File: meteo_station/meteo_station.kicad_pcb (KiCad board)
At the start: 2 copper layers, 110 x 90 mm, 26 parts, among them SW1 SW_SPDT, U1 TP4056, U2 LF33_TO220, U3 ESP32-WROOM, U4 DS18B20, U5 BH1750, U6 BME280

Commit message: Add jumper & version
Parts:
- removed the G*** at (148.6, 99.7)
- removed R6: 0R, Resistor_SMD:R_0603_1608Metric
- added G***: LOGO, meteo_station_footprints:version, F.Cu at (189.2, 83.8)
- added JP1: SolderJumper, Jumper:SolderJumper-2_P1.3mm_Bridged_Pad1.0x1.5mm, F.Cu at (127.0, 99.1)
- moved C2 3.17 mm to (126.4, 120.7)
- moved C3 3.17 mm to (126.4, 115.6)
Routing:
- net GND: track 57.0 -> 63.7 mm
- net OUT+: track 86.8 -> 83.7 mm
- net 3V3: track 175.3 -> 172.1 mm
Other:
- board text removed: "lorem ipsum"

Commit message: Add images
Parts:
- added G***: LOGO, meteo_station_footprints:meteo_station_small, F.Cu at (186.9, 75.9)
- added G***: LOGO, meteo_station_footprints:chmurka2_small, F.Cu at (96.5, 130.0)
- added G***: LOGO, meteo_station_footprints:chmurka, F.Cu at (173.0, 59.7)
- added G***: LOGO, meteo_station_footprints:chmurka, B.Cu at (167.1, 76.2)
- added G***: LOGO, meteo_station_footprints:chmurka, B.Cu at (197.5, 151.6)
- added G***: LOGO, meteo_station_footprints:meteo_station, B.Cu at (149.9, 144.8)
- added G***: LOGO, meteo_station_footprints:chmurka2, B.Cu at (200.7, 100.3)
- added G***: LOGO, meteo_station_footprints:chmurka2, B.Cu at (101.2, 118.7)
- G***: moved to B.Cu
- moved G*** 78.8 mm to (133.3, 139.4), turned to 180 degrees

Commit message: Delete ALL tracks
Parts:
- added C4: 2.2uF, Capacitor_Tantalum_SMD:CP_EIA-3216-18_Kemet-A, F.Cu at (126.4, 80.0)
- added C5: 100nF, Capacitor_SMD:C_0603_1608Metric, F.Cu at (198.8, 108.6)
- C1: value 100nF -> 2200uF; footprint Capacitor_SMD:C_0603_1608Metric -> Capacitor_THT:CP_Radial_D10.0mm_P5.00mm
- C3: value 2.2uF -> 100nF; footprint Capacitor_Tantalum_SMD:CP_EIA-3216-18_Kemet-A -> Capacitor_SMD:C_0603_1608Metric
- moved SC2 69.8 mm to (58.8, 64.8)
- moved D2 57.7 mm to (70.6, 81.9)
- moved SW1 57.5 mm to (47.0, 81.3)
- moved SC1 57.1 mm to (58.8, 73.7)
- moved D1 57.0 mm to (58.8, 81.9)
- moved C2 41.5 mm to (144.1, 83.2)
- moved U2 35.6 mm to (120.1, 85.1)
- moved C1 32.8 mm to (127.6, 72.1)
- moved C3 30.5 mm to (126.4, 85.1)
- moved JP1 1.27 mm to (127.0, 100.3)
- moved U1 1.27 mm to (113.0, 100.3)
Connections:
- C1 pad 1: BAT_V -> 3V3
- C2 pad 1: OUT+ -> BAT_V
- C3 pad 1: 3V3 -> OUT+
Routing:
- net 3V3: track 172.1 -> 0.00 mm
- net Net-(R5-Pad2): track 126.4 -> 0.00 mm, vias 1 -> 0
- net SDA: track 95.4 -> 0.00 mm, vias 1 -> 0
- net Net-(BT1-Pad1): track 94.4 -> 0.00 mm
- net OUT+: track 83.7 -> 0.00 mm, vias 1 -> 0
- net SCL: track 74.2 -> 0.00 mm, vias 1 -> 0
- net Net-(SC1-Pad2): track 74.0 -> 0.00 mm
- net GND: track 63.7 -> 0.00 mm, vias 2 -> 0
- net Net-(D1-Pad1): track 59.7 -> 0.00 mm, vias 2 -> 0
- net BAT_V: track 59.6 -> 0.00 mm
- net Net-(BT1-Pad2): track 45.3 -> 0.00 mm
- net Net-(SW1-Pad2): track 25.7 -> 0.00 mm
- net OUT-: track 13.6 -> 0.00 mm
- net Net-(D2-Pad2): track 11.3 -> 0.00 mm
- net Net-(D1-Pad2): track 11.3 -> 0.00 mm

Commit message: Finished moving
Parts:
- moved SC2 83.5 mm to (120.7, 120.9)
- moved SC1 71.0 mm to (111.8, 120.9)
- moved D2 69.8 mm to (128.9, 120.4)
- moved SW1 66.7 mm to (112.8, 92.1), turned to 180 degrees
- moved D1 58.7 mm to (103.1, 120.4)
- moved C3 23.3 mm to (103.1, 83.8), turned to 180 degrees
- moved U2 9.90 mm to (110.2, 83.8), turned to 0 degrees
- moved JP1 6.38 mm to (127.6, 106.7)
- moved U1 6.35 mm to (113.0, 106.7)
- moved C4 4.96 mm to (123.2, 83.8)
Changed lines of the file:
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@@
   )
   (footprint "meteo_station_footprints:SolarPanel_JST" (layer "F.Cu")
-    (at 58.801 73.66)
+    (at 111.76 120.904)
     (property "Sheetfile" "meteo_station.kicad_sch")
     (property "Sheetname" "")
     (attr through_hole)
-    (fp_text reference "SC1" (at -5.715 0 unlocked) (layer "F.SilkS")
+    (fp_text reference "SC1" (at -0.016 -3.556 unlocked) (layer "F.SilkS")
       (effects (font (size 0.8 0.8) (thickness 0.15)))
     )
-    (fp_text value "Solar_Cell" (at -8.255 -1.905 unlocked) (layer "F.SilkS")
+    (fp_text value "Solar_Cell" (at 0 -3.556 unlocked) (layer "F.SilkS") hide
       (effects (font (size 1 1) (thickness 0.15)))
     )
@@
   )
   (footprint "Package_TO_SOT_THT:TO-220-3_Horizontal_TabDown" (layer "F.Cu")
-    (at 120.055 85.09 90)
+    (at 110.236 83.82)
     (descr "TO-220-3, Horizontal, RM 2.54mm, see https://www.vishay.com/docs/66542/to-220-1.pdf")
     (tags "TO-220-3 Horizontal RM 2.54mm")
@@
     (property "Sheetname" "")
     (attr through_hole)
-    (fp_text reference "U2" (at 8.89 -18.755) (layer "F.SilkS")
+    (fp_text reference "U2" (at -2.032 -20.32 180) (layer "F.SilkS")
       (effects (font (size 0.8 0.8) (thickness 0.15)))
     )
-    (fp_text value "LF33_TO220" (at 2.54 2 90) (layer "F.Fab")
+    (fp_text value "LF33_TO220" (at 2.54 2) (layer "F.Fab")
       (effects (font (size 1 1) (thickness 0.15)))
     )
-    (fp_text user "${REFERENCE}" (at 2.54 -20.58 90) (layer "F.Fab")
+    (fp_text user "${REFERENCE}" (at 2.54 -20.58) (layer "F.Fab")
       (effects (font (size 1 1) (thickness 0.15)))
     )
@@
     (fp_line (start -2.46 -3.81) (end -2.46 -13.06) (layer "F.Fab") (width 0.1))
     (fp_circle (center 2.54 -16.66) (end 4.39 -16.66) (layer "F.Fab") (width 0.1) (fill none))
-    (pad "" np_thru_hole oval locked (at 2.54 -16.66 90) (size 3.5 3.5) (drill 3.5) (layers *.Cu *.Mask))
-    (pad "1" thru_hole rect locked (at 0 0 90) (size 1.905 2) (drill 1.1) (layers *.Cu *.Mask)
+    (pad "" np_thru_hole oval locked (at 2.54 -16.66) (size 3.5 3.5) (drill 3.5) (layers *.Cu *.Mask))
+    (pad "1" thru_hole rect locked (at 0 0) (size 1.905 2) (drill 1.1) (layers *.Cu *.Mask)
       (net 11 "OUT+") (pinfunction "VI") (pintype "passive"))
-    (pad "2" thru_hole oval locked (at 2.54 0 90) (size 1.905 2) (drill 1.1) (layers *.Cu *.Mask)
+    (pad "2" thru_hole oval locked (at 2.54 0) (size 1.905 2) (drill 1.1) (layers *.Cu *.Mask)
       (net 39 "GND") (pinfunction "GND") (pintype "power_in"))
-    (pad "3" thru_hole oval locked (at 5.08 0 90) (size 1.905 2) (drill 1.1) (layers *.Cu *.Mask)
+    (pad "3" thru_hole oval locked (at 5.08 0) (size 1.905 2) (drill 1.1) (layers *.Cu *.Mask)
       (net 3 "3V3") (pinfunction "VO") (pintype "passive"))
     (model "${KICAD6_3DMODEL_DIR}/Package_TO_SOT_THT.3dshapes/TO-220-3_Horizontal_TabDown.wrl"
@@
   )
   (footprint "Diode_SMD:D_SMB" (layer "F.Cu")
-    (at 70.621 81.915 180)
+    (at 128.905 120.396 180)
     (descr "Diode SMB (DO-214AA)")
     (tags "Diode SMB (DO-214AA)")
@@
   )
   (footprint "meteo_station_footprints:MTS102" (layer "F.Cu")
-    (at 46.99 81.28 90)
+    (at 112.776 92.075 180)
     (property "Sheetfile" "meteo_station.kicad_sch")
     (property "Sheetname" "")
     (attr through_hole)
-    (fp_text reference "SW1" (at -7.62 3.81 unlocked) (layer "F.SilkS")
+    (fp_text reference "SW1" (at 4.191 5.08 unlocked) (layer "F.SilkS")
       (effects (font (size 0.8 0.8) (thickness 0.15)) (justify right))
     )
-    (fp_text value "SW_SPDT" (at 0 -5.715 90 unlocked) (layer "F.Fab")
+    (fp_text value "SW_SPDT" (at -0.635 -5.715 180 unlocked) (layer "F.Fab")
       (effects (font (size 1 1) (thickness 0.15)))
     )
-    (fp_text user "${REFERENCE}" (at 0 -6.985 90 unlocked) (layer "F.Fab")
+    (fp_text user "${REFERENCE}" (at -0.635 -6.985 180 unlocked) (layer "F.Fab")
       (effects (font (size 1 1) (thickness 0.15)))
     )
     (fp_rect (start -6.6 -4) (end 6.6 4) (layer "F.SilkS") (width 0.2) (fill none))
-    (pad "1" thru_hole oval (at -4.7 0 90) (size 3.2 6.5) (drill oval 2 3) (layers *.Cu *.Mask)
+    (pad "1" thru_hole oval (at -4.7 0 180) (size 3.2 6.5) (drill oval 2 3) (layers *.Cu *.Mask)
       (net 11 "OUT+") (pinfunction "A") (pintype "passive"))
-    (pad "2" thru_hole oval (at 0 0 90) (size 3.2 6.5) (drill oval 2 3) (layers *.Cu *.Mask)
+    (pad "2" thru_hole oval (at 0 0 180) (size 3.2 6.5) (drill oval 2 3) (layers *.Cu *.Mask)
       (net 7 "Net-(SW1-Pad2)") (pinfunction "B") (pintype "passive"))
-    (pad "3" thru_hole oval (at 4.7 0 90) (size 3.2 6.5) (drill oval 2 3) (layers *.Cu *.Mask)
+    (pad "3" thru_hole oval (at 4.7 0 180) (size 3.2 6.5) (drill oval 2 3) (layers *.Cu *.Mask)
       (net 8 "unconnected-(SW1-Pad3)") (pinfunction "C") (pintype "passive+no_connect"))
   )
@@
   )
   (footprint "Jumper:SolderJumper-2_P1.3mm_Bridged_Pad1.0x1.5mm" (layer "F.Cu")
-    (at 127 100.33)
+    (at 127.635 106.68)
     (descr "SMD Solder Jumper, 1x1.5mm Pads, 0.3mm gap, bridged with 1 copper strip")
     (tags "net tie solder jumper bridged")
@@
   )
   (footprint "Capacitor_Tantalum_SMD:CP_EIA-3216-18_Kemet-A" (layer "F.Cu")
-    (at 126.365 80.01)
+    (at 123.19 83.82)
     (descr "Tantalum Capacitor SMD Kemet-A (3216-18 Metric), IPC_7351 nominal, (Body size from: http://www.kemet.com/Lists/ProductCatalog/Attachments/253/KEM_TC101_STD.pdf), generated with kicad-footprint-generator")
     (tags "capacitor tantalum")
@@
   )
   (footprint "Capacitor_SMD:C_0603_1608Metric" (layer "F.Cu")
-    (at 126.365 85.09)
+    (at 103.124 83.82 180)
     (descr "Capacitor SMD 0603 (1608 Metric), square (rectangular) end terminal, IPC_7351 nominal, (Body size source: IPC-SM-782 page 76, https://www.pcb-3d.com/wordpress/wp-content/uploads/ipc-sm-782a_amendment_1_and_2.pdf), generated with kicad-footprint-generator")
     (tags "capacitor")
@@
     (property "Sheetname" "")
     (attr smd)
-    (fp_text reference "C3" (at 0 -1.43) (layer "F.SilkS")
+    (fp_text reference "C3" (at 0 1.27) (layer "F.SilkS")
       (effects (font (size 0.8 0.8) (thickness 0.15)))
     )
@@
     (fp_line (start -0.8 -0.4) (end 0.8 -0.4) (layer "F.Fab") (width 0.1))
     (fp_line (start -0.8 0.4) (end -0.8 -0.4) (layer "F.Fab") (width 0.1))
-    (pad "1" smd roundrect locked (at -0.775 0) (size 0.9 0.95) (layers "F.Cu" "F.Paste" "F.Mask") (roundrect_rratio 0.25)
+    (pad "1" smd roundrect locked (at -0.775 0 180) (size 0.9 0.95) (layers "F.Cu" "F.Paste" "F.Mask") (roundrect_rratio 0.25)
       (net 11 "OUT+") (pintype "passive"))
-    (pad "2" smd roundrect locked (at 0.775 0) (size 0.9 0.95) (layers "F.Cu" "F.Paste" "F.Mask") (roundrect_rratio 0.25)
+    (pad "2" smd roundrect locked (at 0.775 0 180) (size 0.9 0.95) (layers "F.Cu" "F.Paste" "F.Mask") (roundrect_rratio 0.25)
       (net 39 "GND") (pintype "passive"))
     (model "${KICAD6_3DMODEL_DIR}/Capacitor_SMD.3dshapes/C_0603_1608Metric.wrl"
@@
   )
   (footprint "meteo_station_footprints:TP4056" (layer "F.Cu")
-    (at 113.03 100.33)
+    (at 113.03 106.68)
     (property "Sheetfile" "meteo_station.kicad_sch")
     (property "Sheetname" "")
     (attr through_hole)
-    (fp_text reference "U1" (at 12.5 9.525 unlocked) (layer "F.SilkS")
+    (fp_text reference "U1" (at -11.049 -9.398 unlocked) (layer "F.SilkS")
       (effects (font (size 0.8 0.8) (thickness 0.15)) (justify right))
     )
@@
   )
   (footprint "Diode_SMD:D_SMB" (layer "F.Cu")
-    (at 58.801 81.915 180)
+    (at 103.124 120.396 180)
     (descr "Diode SMB (DO-214AA)")
     (tags "Diode SMB (DO-214AA)")
@@
   )
   (footprint "meteo_station_footprints:SolarPanel_JST" (layer "F.Cu")
-    (at 58.801 64.77)
+    (at 120.65 120.904)
     (property "Sheetfile" "meteo_station.kicad_sch")
     (property "Sheetname" "")
     (attr through_hole)
-    (fp_text reference "SC2" (at -5.715 0 unlocked) (layer "F.SilkS")
+    (fp_text reference "SC2" (at -0.016 -3.556 unlocked) (layer "F.SilkS")
       (effects (font (size 0.8 0.8) (thickness 0.15)))
     )
-    (fp_text value "Solar_Cell" (at -8.255 -1.905 unlocked) (layer "F.SilkS")
+    (fp_text value "Solar_Cell" (at 0 -3.556 unlocked) (layer "F.SilkS") hide
       (effects (font (size 1 1) (thickness 0.15)))
     )

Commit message: new tracks
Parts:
- moved R5 38.3 mm to (132.7, 87.6)
- moved C2 27.6 mm to (167.0, 98.6), turned to -90 degrees
- moved R3 5.54 mm to (167.0, 87.6)
- moved R4 5.54 mm to (167.0, 93.2)
- turned R2 to -90 degrees
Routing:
- net 3V3: track 0.00 -> 166.9 mm
- net SDA: track 0.00 -> 106.3 mm, vias 0 -> 2
- net Net-(R5-Pad2): track 0.00 -> 100.3 mm
- net Net-(BT1-Pad1): track 0.00 -> 87.8 mm
- net SCL: track 0.00 -> 87.6 mm, vias 0 -> 1
- net BAT_V: track 0.00 -> 70.5 mm, vias 0 -> 1
- net Net-(D1-Pad1): track 0.00 -> 66.7 mm
- net Net-(BT1-Pad2): track 0.00 -> 45.5 mm
- net OUT+: track 0.00 -> 34.1 mm
- net Net-(SC1-Pad2): track 0.00 -> 27.8 mm
- net OUT-: track 0.00 -> 17.6 mm
- net Net-(SW1-Pad2): track 0.00 -> 15.7 mm
- net Net-(D1-Pad2): track 0.00 -> 13.1 mm
- net Net-(D2-Pad2): track 0.00 -> 10.5 mm

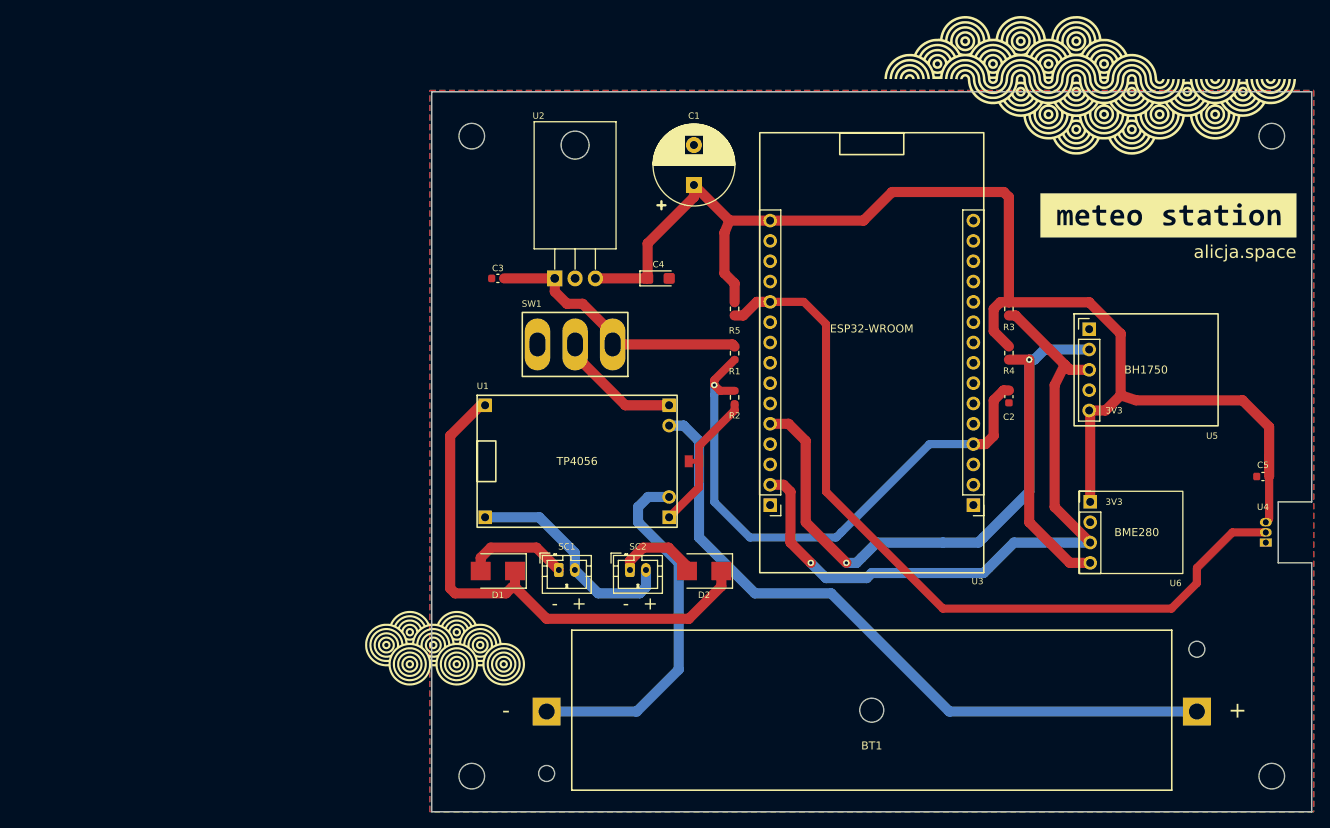
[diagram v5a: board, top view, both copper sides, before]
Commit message: Very thick routes
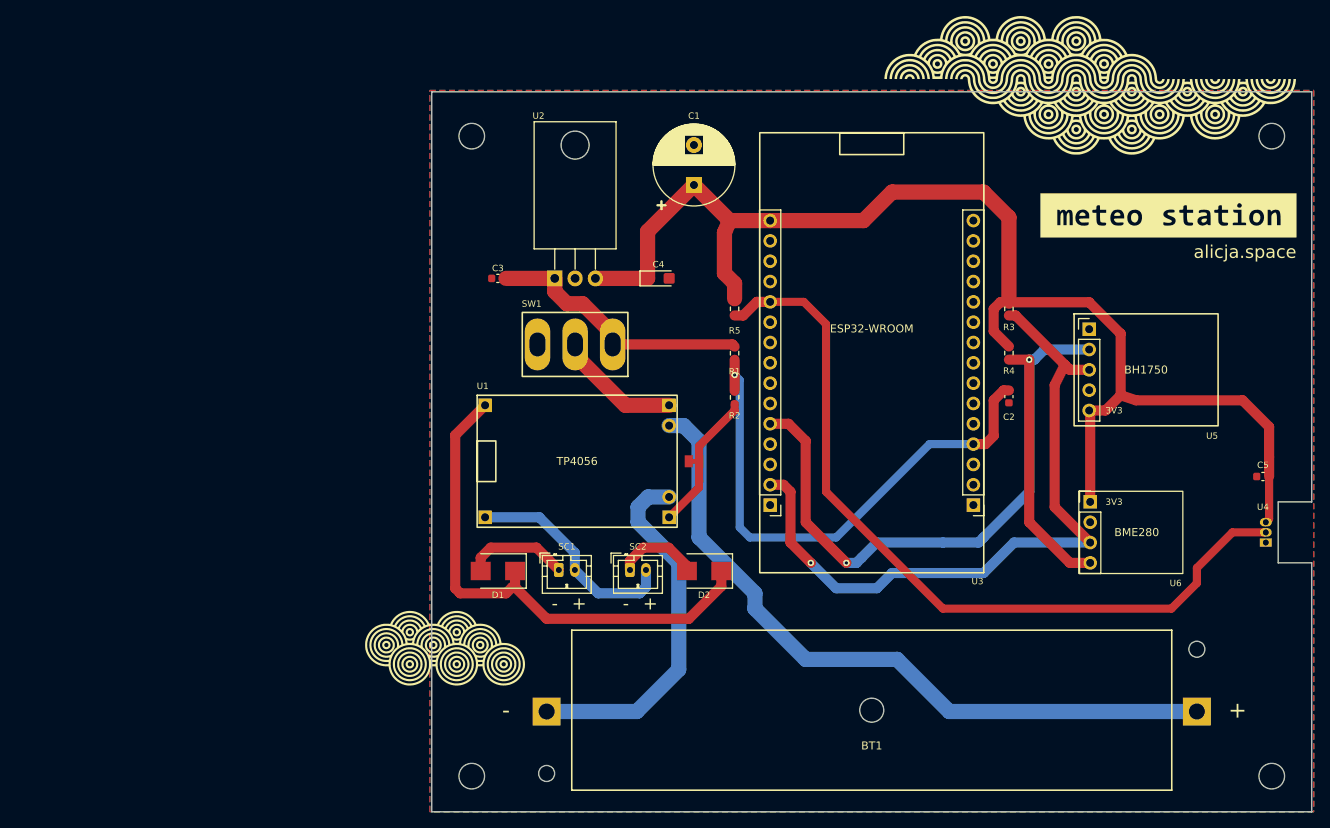
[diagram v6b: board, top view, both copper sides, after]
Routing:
- net BAT_V: track 70.5 -> 67.6 mm
- net 3V3: track 166.9 -> 164.9 mm
- net Net-(D1-Pad1): track 66.7 -> 65.5 mm
- net Net-(BT1-Pad1): track 87.8 -> 89.0 mm
- net SCL: track 87.6 -> 88.7 mm

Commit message: Typo & label
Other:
- board text added: "3V3"
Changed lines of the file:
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@@
       (outputformat 1)
       (mirror false)
-      (drillshape 1)
+      (drillshape 0)
       (scaleselection 1)
-      (outputdirectory "")
+      (outputdirectory "../gerbers/")
     )
   )
@@
     (fp_line (start -2.966 2.165) (end 2.934 2.165) (layer "F.Fab") (width 0.1))
     (fp_line (start -2.966 -2.335) (end -2.966 2.165) (layer "F.Fab") (width 0.1))
-    (pad "1" thru_hole roundrect (at -1.016 -0.635) (size 1.2 1.75) (drill 0.75) (layers *.Cu *.Mask) (roundrect_rratio 0.208333)
+    (pad "1" thru_hole roundrect (at -1.016 -0.635) (size 1.2 1.75) (drill 0.75) (layers *.Cu *.Mask) (roundrect_rratio 0.2083333333)
       (net 13 "Net-(D1-Pad2)") (pinfunction "+") (pintype "passive"))
     (pad "2" thru_hole oval (at 0.984 -0.635) (size 1.2 1.75) (drill 0.75) (layers *.Cu *.Mask)
@@
     (fp_line (start -1.6 0.8) (end 1.6 0.8) (layer "F.Fab") (width 0.1))
     (fp_line (start 1.6 -0.8) (end -1.2 -0.8) (layer "F.Fab") (width 0.1))
-    (pad "1" smd roundrect locked (at -1.35 0) (size 1.4 1.35) (layers "F.Cu" "F.Paste" "F.Mask") (roundrect_rratio 0.185185)
+    (pad "1" smd roundrect locked (at -1.35 0) (size 1.4 1.35) (layers "F.Cu" "F.Paste" "F.Mask") (roundrect_rratio 0.1851851852)
       (net 3 "3V3") (pintype "passive"))
-    (pad "2" smd roundrect locked (at 1.35 0) (size 1.4 1.35) (layers "F.Cu" "F.Paste" "F.Mask") (roundrect_rratio 0.185185)
+    (pad "2" smd roundrect locked (at 1.35 0) (size 1.4 1.35) (layers "F.Cu" "F.Paste" "F.Mask") (roundrect_rratio 0.1851851852)
       (net 39 "GND") (pintype "passive"))
     (model "${KICAD6_3DMODEL_DIR}/Capacitor_Tantalum_SMD.3dshapes/CP_EIA-3216-18_Kemet-A.wrl"
@@
     (fp_line (start -3.376 -2.745) (end -3.376 -1.495) (layer "F.Fab") (width 0.1))
     (fp_line (start -2.126 -2.745) (end -3.376 -2.745) (layer "F.Fab") (width 0.1))
-    (pad "1" thru_hole roundrect (at -1.016 -0.635) (size 1.2 1.75) (drill 0.75) (layers *.Cu *.Mask) (roundrect_rratio 0.208333)
+    (pad "1" thru_hole roundrect (at -1.016 -0.635) (size 1.2 1.75) (drill 0.75) (layers *.Cu *.Mask) (roundrect_rratio 0.2083333333)
       (net 14 "Net-(D2-Pad2)") (pinfunction "+") (pintype "passive"))
     (pad "2" thru_hole oval (at 0.984 -0.635) (size 1.2 1.75) (drill 0.75) (layers *.Cu *.Mask)
@@
   (gr_line (start 204.86 150.5) (end 204.86 119.38) (layer "Edge.Cuts") (width 0.1))
   (gr_line (start 204.86 60.5) (end 204.86 111.76) (layer "Edge.Cuts") (width 0.1))
+  (gr_text "3V3" (at 139.192 76.708) (layer "F.SilkS")
+    (effects (font (size 0.8 0.8) (thickness 0.15)) (justify left))
+  )
   (gr_text "alicja.space" (at 202.946 80.518) (layer "F.SilkS")
     (effects (font (size 1.6 1.6) (thickness 0.2)) (justify right))
